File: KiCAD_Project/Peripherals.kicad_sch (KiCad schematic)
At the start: 23 parts, among them J10 HMC Breakout Pins, J11 1-0001555, J12 1-0001555, J13 HMC Breakout Pins, Q1 1-0001548, Q2 1-0001214, U7 1-0001535, U8 1-0001471, U9 1-0001543

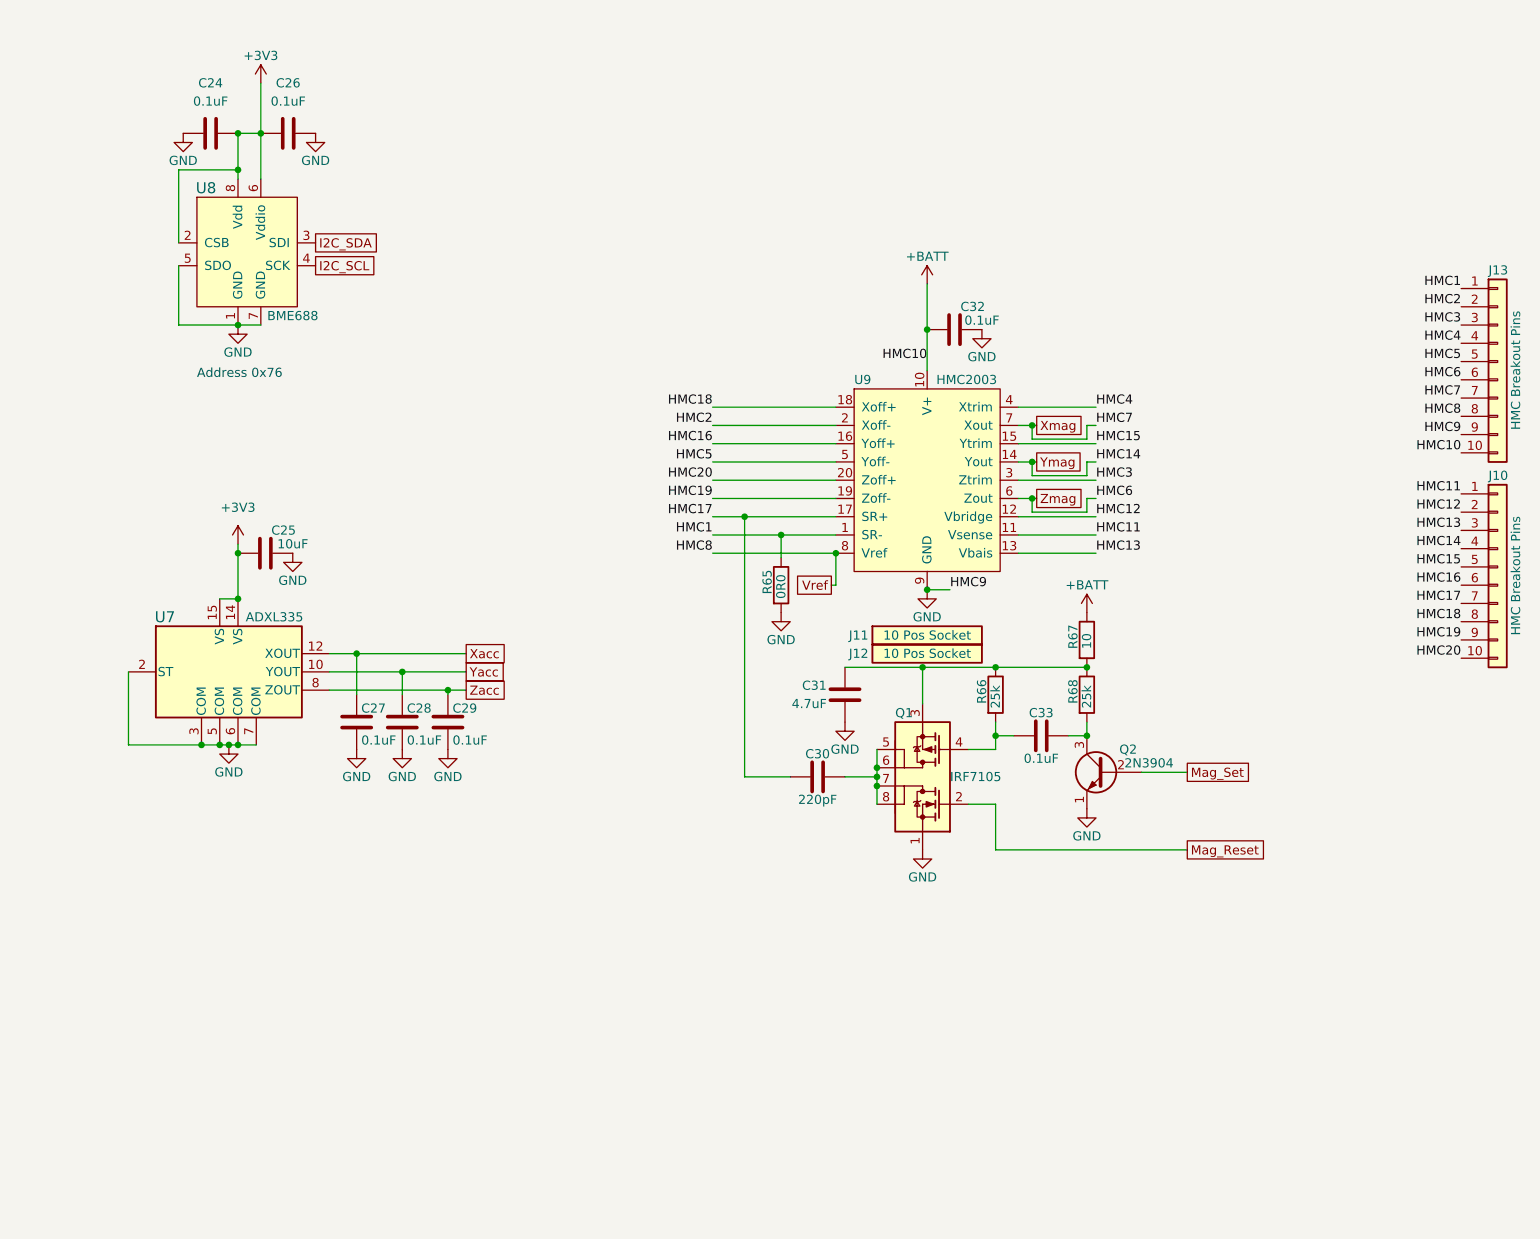
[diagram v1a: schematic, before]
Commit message: Fixed Issue #4 (Added Buffers to Accel Output)
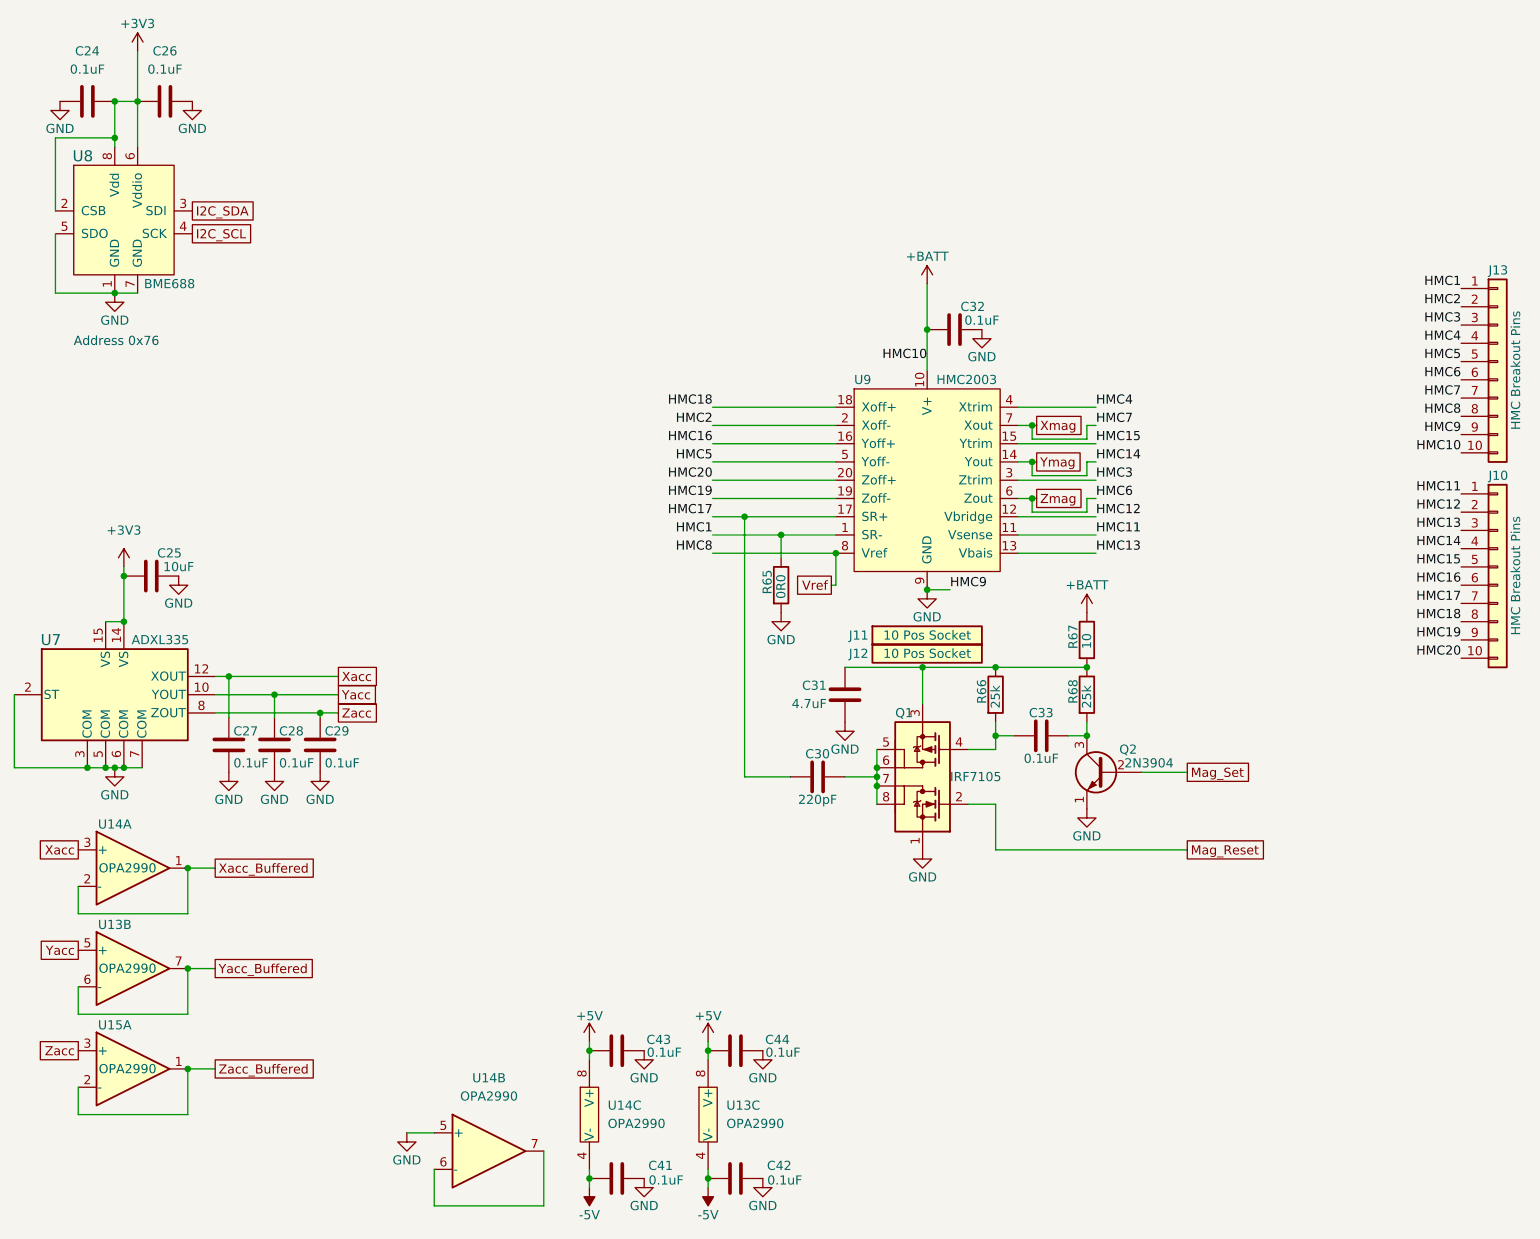
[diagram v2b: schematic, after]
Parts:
- added C41, C42, C43, C44: 1-0000007, capacitors_0603:1-0000007, symbol capacitors_0603:1-0000007
- added U13, U14, U15: 1-0000264, amplifiers:1-0000264, symbol amplifiers:1-0000264
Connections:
- net GND: now also C41.2, C42.2, C43.2, C44.2, U14.5 (+)
- net Xacc: now also U14.3 (+)
- net Yacc: now also U13.5 (+)
- net Zacc: now also U15.3 (+)
- new net: U14.6 (-), U14.7
- new net +5V: C43.1, C44.1, U13.8 (V+), U14.8 (V+)
- new net -5V: C41.1, C42.1, U13.4 (V-), U14.4 (V-)
- new net Xacc_Buffered: U14.1, U14.2 (-)
- new net Yacc_Buffered: U13.6 (-), U13.7
- new net Zacc_Buffered: U15.1, U15.2 (-)
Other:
- moved on the sheet: C24, C25, C26, C27, C28, C29, U7, U8

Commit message: Fixed Issue #3 (ADC Cleanup and Removed Second ADC/MAG Component)
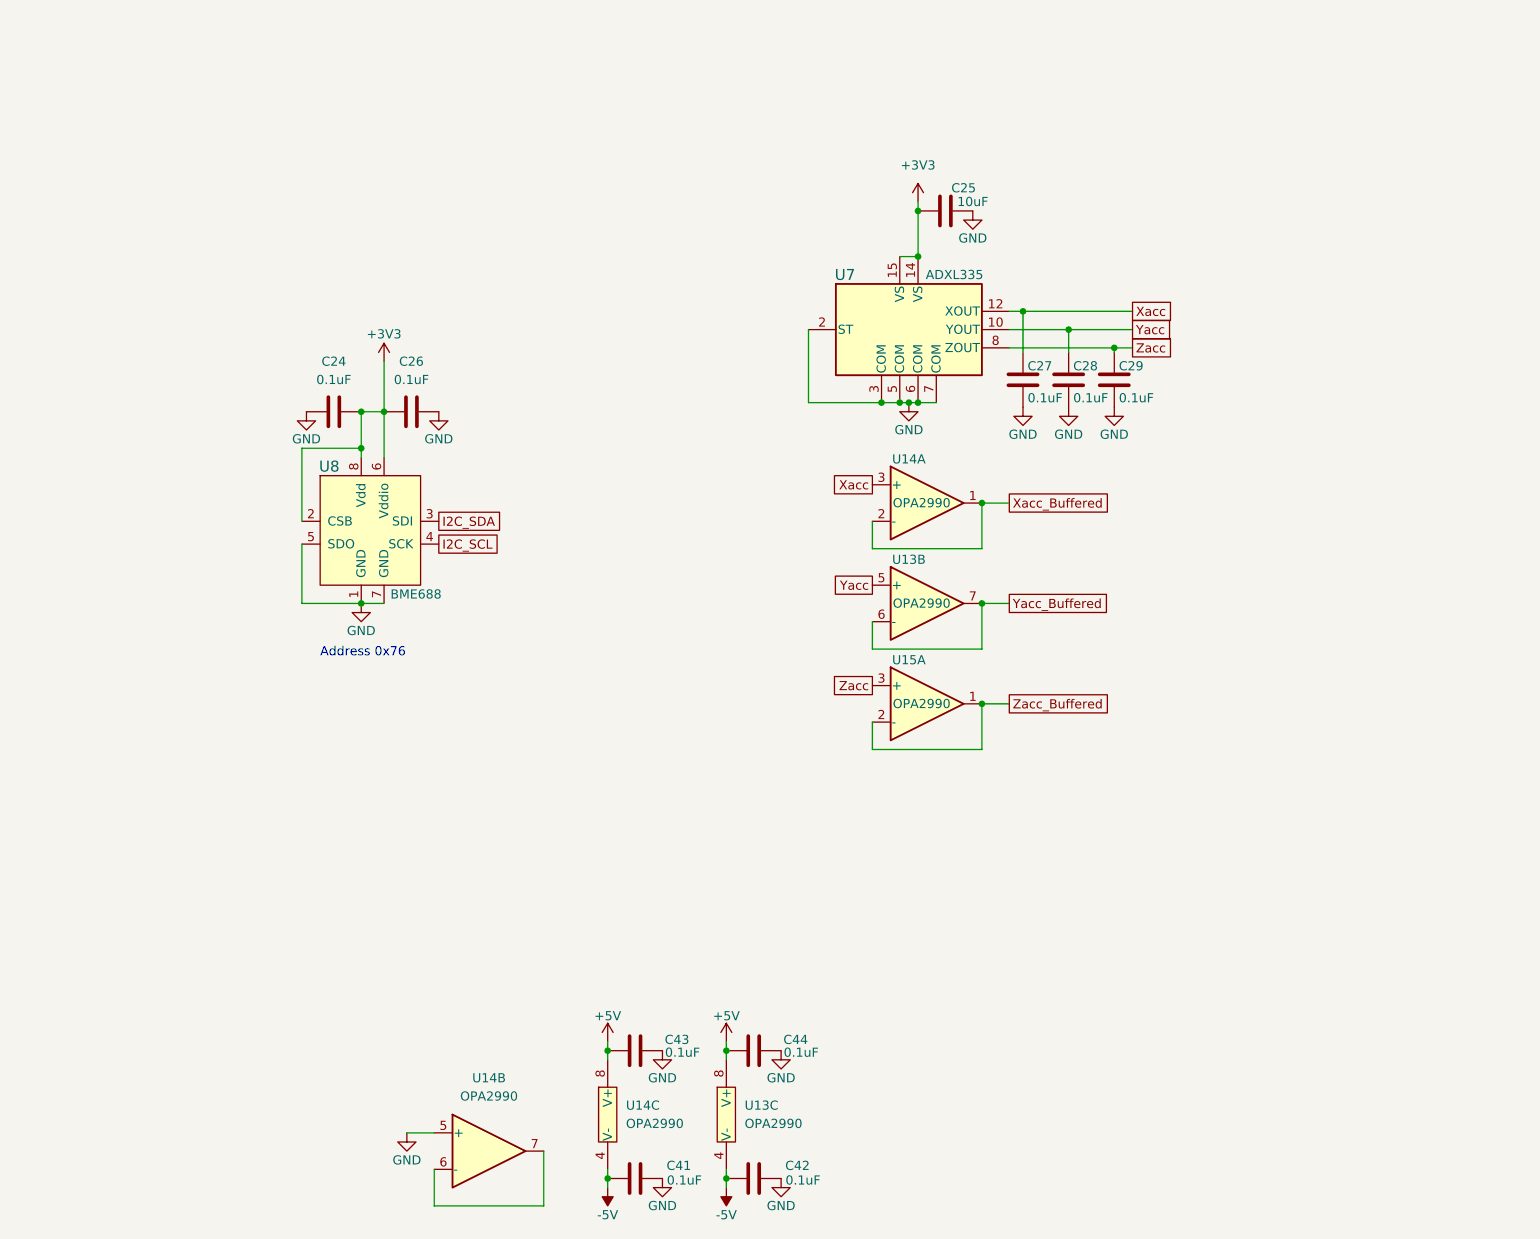
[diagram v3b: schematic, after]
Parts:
- removed C30: 1-0000322, capacitors_0603:1-0000322, symbol capacitors_0603:1-0000322
- removed C31: 1-0000136, capacitors_1206:1-0000136, symbol capacitors_1206:1-0000136
- removed C32, C33: 1-0000007, capacitors_0603:1-0000007, symbol capacitors_0603:1-0000007
- removed J10, J13: HMC Breakout Pins, Connector_PinHeader_2.54mm:PinHeader_1x10_P2.54mm_Vertical, symbol Connector_Generic:Conn_01x10
- removed J11, J12: 1-0001555, connectors:1-0001555, symbol connectors:1-0001555
- removed Q1: 1-0001548, mosfets:1-0001548, symbol mosfets:1-0001548
- removed Q2: 1-0001214, transistors:1-0001214, symbol transistors:1-0001214
- removed R65: 1-0000006, resistors_0603:1-0000006, symbol resistors_0603:1-0000006
- removed R66, R68: 1-0001549, resistors_0805:1-0001549, symbol resistors_0805:1-0001549
- removed R67: 1-0001528, resistors_0603:1-0001528, symbol resistors_0603:1-0001528
- removed U9: 1-0001543, sensors:1-0001543, symbol sensors:1-0001543
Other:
- moved on the sheet: C24, C25, C26, C27, C28, C29, C41, C42, C43, U13B, U13C, U14A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

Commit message: Schematic ERC Issue Cleanup
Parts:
- removed U13, U14, U15: 1-0000264, amplifiers:1-0000264, symbol amplifiers:1-0000264
- added U5, U9: 1-0000264, amplifiers:1-0000264, symbol amplifiers:1-0000264
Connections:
- net +5V: now also U5.8 (V+), U9.8 (V+)
- net -5V: now also U5.4 (V-), U9.4 (V-)
- net GND: now also U9.5 (+)
- net Xacc: now also U5.3 (+)
- net Xacc_Buffered: now also U5.1, U5.2 (-)
- net Yacc: now also U5.5 (+)
- net Yacc_Buffered: now also U5.6 (-), U5.7
- net Zacc: now also U9.3 (+)
- net Zacc_Buffered: now also U9.1, U9.2 (-)
- new net: U9.6 (-), U9.7
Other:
- moved on the sheet: C26

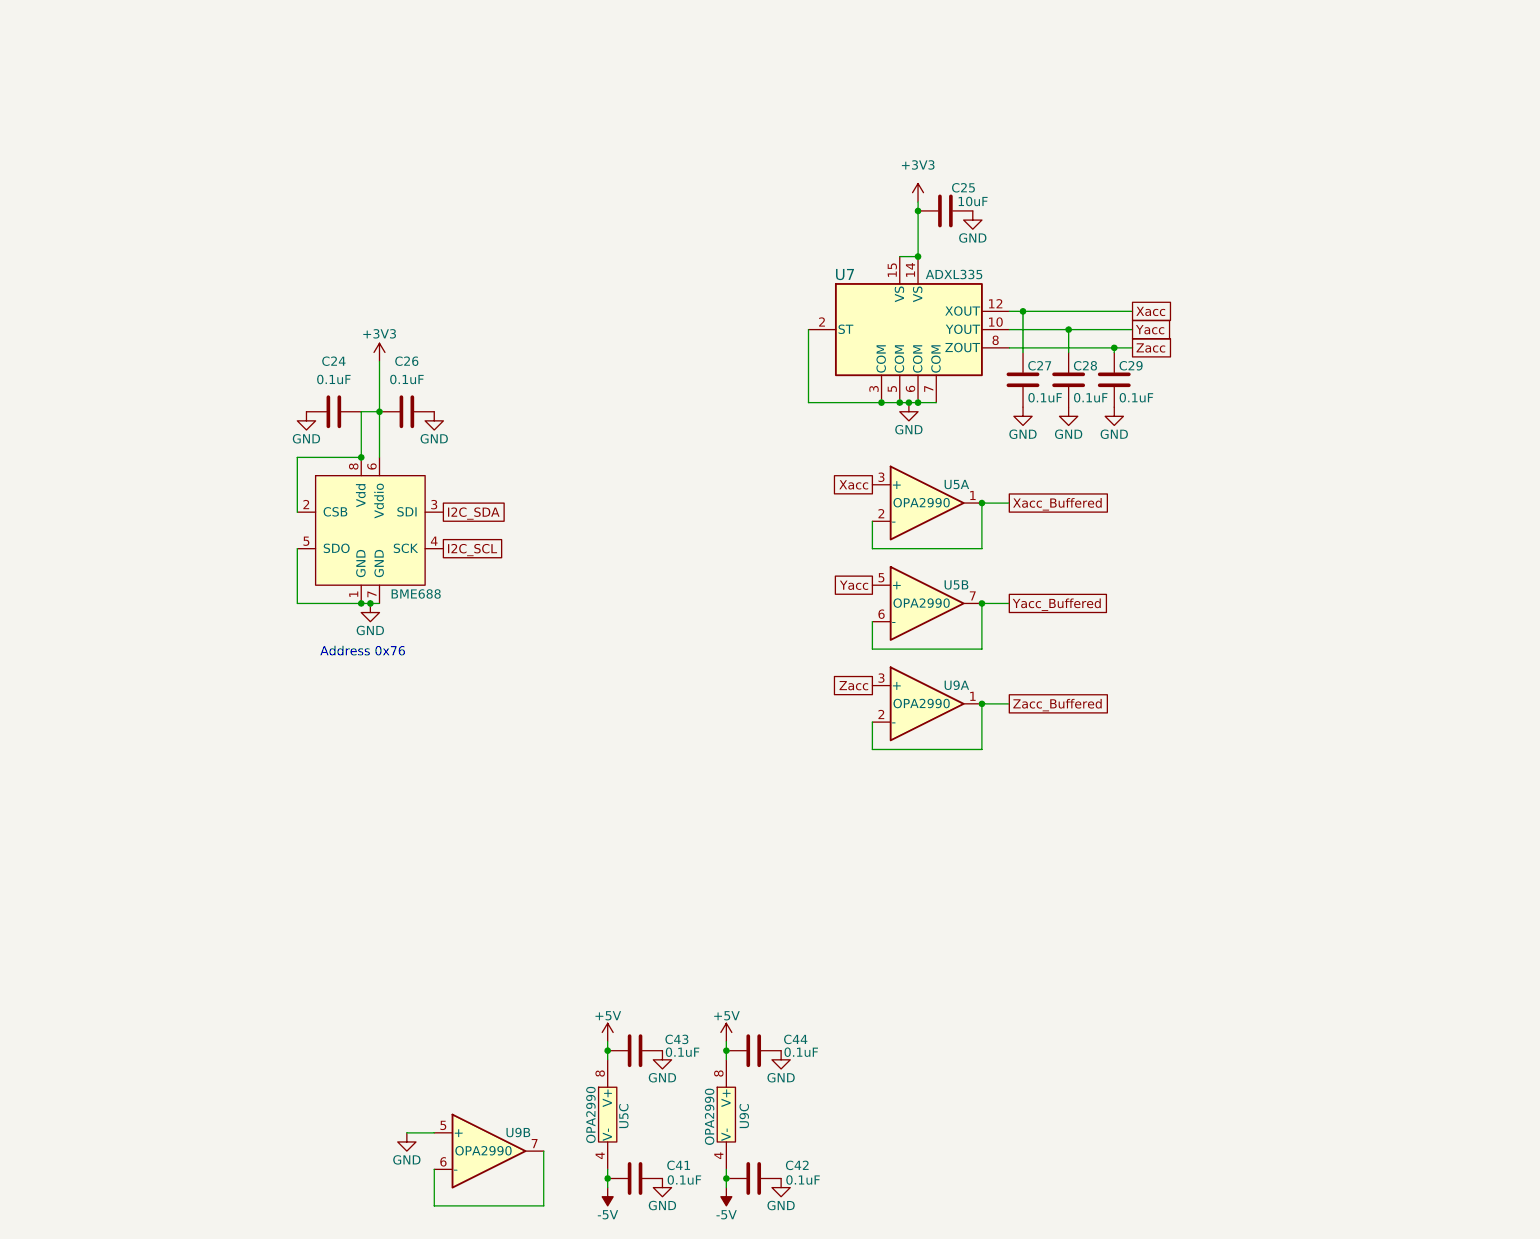
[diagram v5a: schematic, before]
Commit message: Revised Layout for Rev2.0 Changes
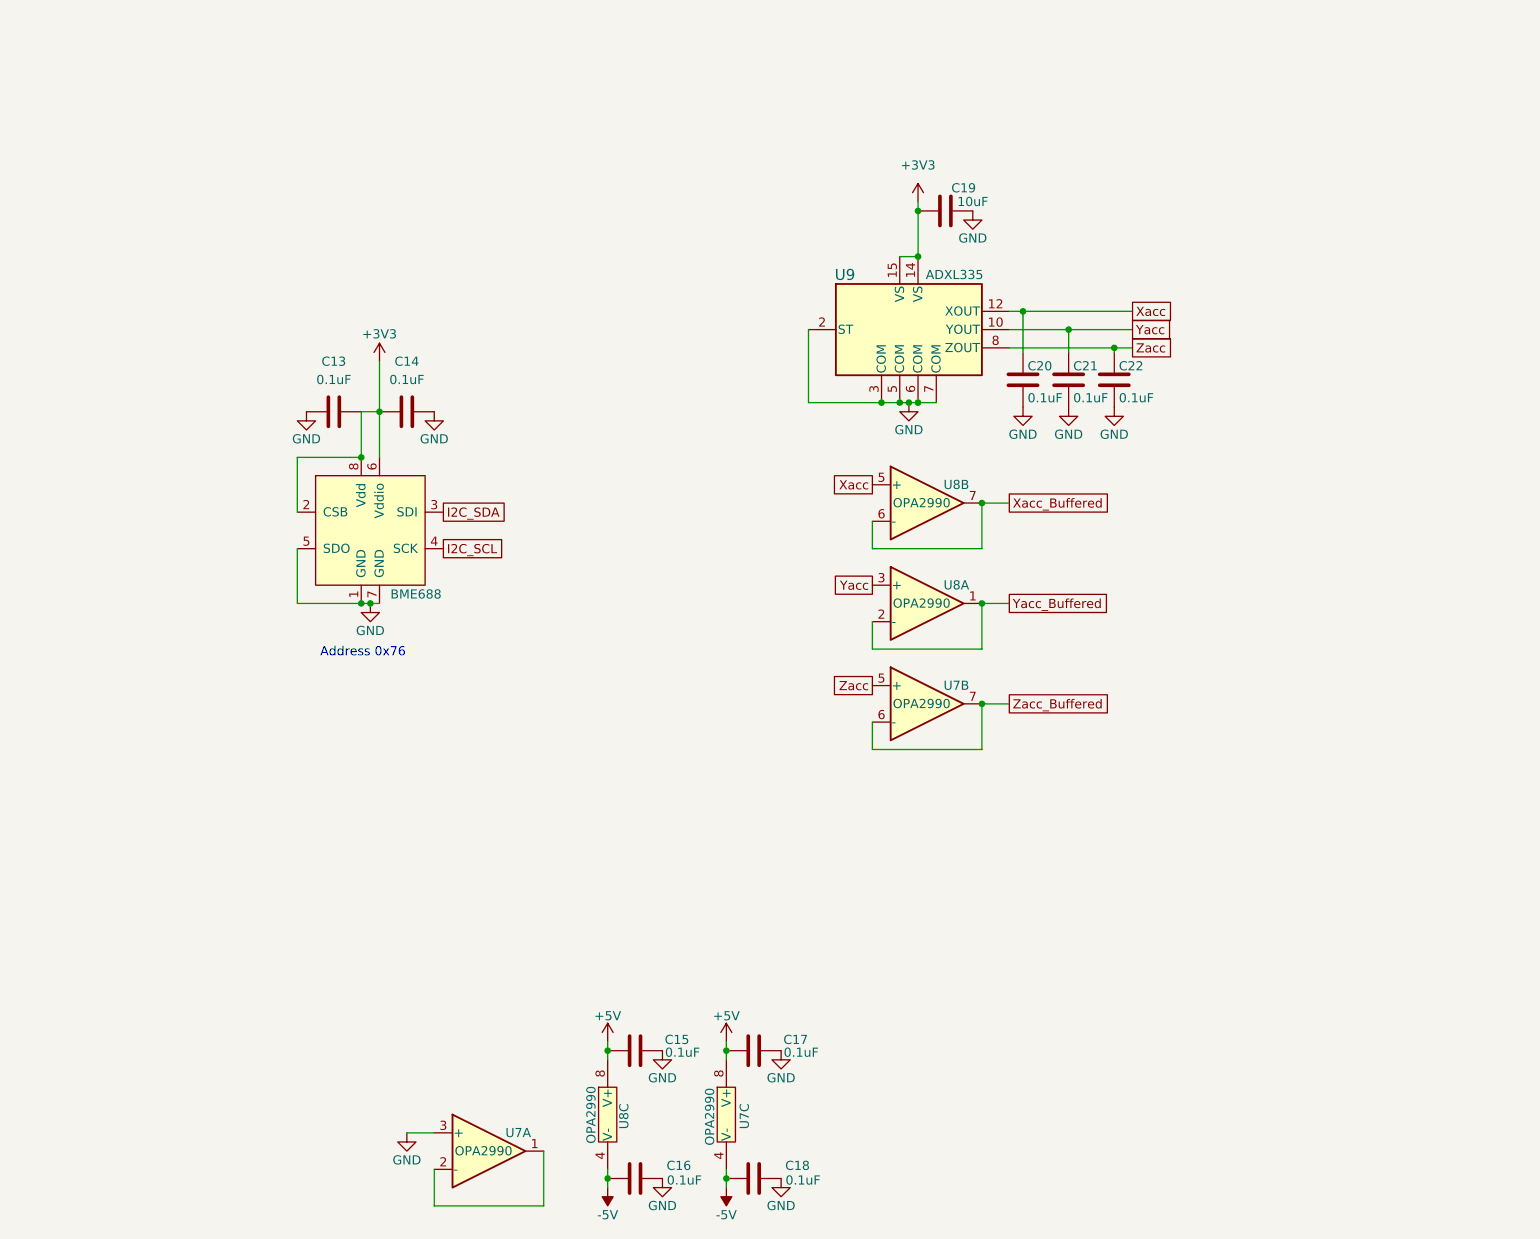
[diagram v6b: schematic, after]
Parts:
- renumbered C24 to C13, C26 to C14, C43 to C15, C41 to C16, C44 to C17, C42 to C18, C25 to C19, C27 to C20, C28 to C21, C29 to C22, U8 to U6, U9 to U7, U5 to U8, U7 to U9
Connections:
- net GND: now also U7.3 (+); no longer U7.5 (+)
- net Xacc: now also U8.5 (+); no longer U8.3 (+)
- net Xacc_Buffered: now also U8.6 (-), U8.7; no longer U8.1, U8.2 (-)
- net Yacc: now also U8.3 (+); no longer U8.5 (+)
- net Yacc_Buffered: now also U8.1, U8.2 (-); no longer U8.6 (-), U8.7
- net Zacc: now also U7.5 (+); no longer U7.3 (+)
- net Zacc_Buffered: now also U7.6 (-), U7.7; no longer U7.1, U7.2 (-)
- new net: U7.1, U7.2 (-)
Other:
- moved on the sheet: U7A, U7B, U8A, U8B
